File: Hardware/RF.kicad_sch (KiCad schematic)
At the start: 0 parts

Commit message: Checkpoint
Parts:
- added C2, C3, C4, C6, C7: 100nF, symbol Device:C_Small
- added C5: 47pF, symbol Device:C_Small
- added U3: SX1276, Package_DFN_QFN:QFN-28-1EP_6x6mm_P0.65mm_EP4.8x4.8mm, symbol RF:SX1276
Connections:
- new net: C6.1, U3.4 (VR_DIG)
- new net: C7.1, U3.2 (VR_ANA)
- new net DIO0: U3.8 (DIO0)
- new net DIO1: U3.9 (DIO1)
- new net DIO2: U3.10 (DIO2)
- new net DIO3: U3.11 (DIO3)
- new net DIO4: U3.12 (DIO4)
- new net DIO5: U3.13 (DIO5)
- new net GND: C2.1, C3.1, C4.1, C5.2, C6.2, C7.2, U3.15 (GND), U3.23 (GND), U3.26 (GND), U3.29 (GND)
- new net MISO: U3.17 (MISO)
- new net MOSI: U3.18 (MOSI)
- new net NSS: U3.19 (NSS)
- new net SCK: U3.16 (SCK)
- new net VDD: C2.2, C3.2, C4.2, C5.1, U3.14 (VBAT_DIG), U3.24 (VBAT_RF), U3.3 (VBAT_ANA)
- new net ~{RESET}: U3.7 (~{RESET})

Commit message: Checkpoint
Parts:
- renumbered C4 to C901, C3 to C902, C2 to C903, C5 to C904, C7 to C905, C6 to C906, U3 to U901
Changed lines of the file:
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@@
   (symbol (lib_id "Device:C_Small") (at 124.46 48.26 90) (unit 1)
     (in_bom yes) (on_board yes) (dnp no) (fields_autoplaced)
-    (property "Reference" "C3" (at 124.4663 41.91 90)
+    (property "Reference" "C902" (at 124.4663 41.91 90)
       (effects (font (size 1.27 1.27)))
     )
@@
       (project "Avionus_Flight_Controller"
         (path "/ddc7e940-0588-4587-8902-8ced9e615ace/a9aaa4a3-7ef9-4aeb-9917-54b44867eb01"
-          (reference "C3") (unit 1)
+          (reference "C902") (unit 1)
         )
       )
@@
   (symbol (lib_id "Device:C_Small") (at 144.78 58.42 90) (unit 1)
     (in_bom yes) (on_board yes) (dnp no) (fields_autoplaced)
-    (property "Reference" "C6" (at 144.7863 52.07 90)
+    (property "Reference" "C906" (at 144.7863 52.07 90)
       (effects (font (size 1.27 1.27)))
     )
@@
       (project "Avionus_Flight_Controller"
         (path "/ddc7e940-0588-4587-8902-8ced9e615ace/a9aaa4a3-7ef9-4aeb-9917-54b44867eb01"
-          (reference "C6") (unit 1)
+          (reference "C906") (unit 1)
         )
       )
@@
   (symbol (lib_id "RF:SX1276") (at 134.62 88.9 0) (unit 1)
     (in_bom yes) (on_board yes) (dnp no) (fields_autoplaced)
-    (property "Reference" "U3" (at 136.5759 116.84 0)
+    (property "Reference" "U901" (at 136.5759 116.84 0)
       (effects (font (size 1.27 1.27)) (justify left))
     )
@@
       (project "Avionus_Flight_Controller"
         (path "/ddc7e940-0588-4587-8902-8ced9e615ace/a9aaa4a3-7ef9-4aeb-9917-54b44867eb01"
-          (reference "U3") (unit 1)
+          (reference "U901") (unit 1)
         )
       )
@@
   (symbol (lib_id "Device:C_Small") (at 124.46 58.42 90) (unit 1)
     (in_bom yes) (on_board yes) (dnp no) (fields_autoplaced)
-    (property "Reference" "C2" (at 124.4663 52.07 90)
+    (property "Reference" "C903" (at 124.4663 52.07 90)
       (effects (font (size 1.27 1.27)))
     )
@@
       (project "Avionus_Flight_Controller"
         (path "/ddc7e940-0588-4587-8902-8ced9e615ace/a9aaa4a3-7ef9-4aeb-9917-54b44867eb01"
-          (reference "C2") (unit 1)
+          (reference "C903") (unit 1)
         )
       )
@@
   (symbol (lib_id "Device:C_Small") (at 124.46 38.1 90) (unit 1)
     (in_bom yes) (on_board yes) (dnp no) (fields_autoplaced)
-    (property "Reference" "C4" (at 124.4663 31.75 90)
+    (property "Reference" "C901" (at 124.4663 31.75 90)
       (effects (font (size 1.27 1.27)))
     )
@@
       (project "Avionus_Flight_Controller"
         (path "/ddc7e940-0588-4587-8902-8ced9e615ace/a9aaa4a3-7ef9-4aeb-9917-54b44867eb01"
-          (reference "C4") (unit 1)
+          (reference "C901") (unit 1)
         )
       )
@@
   (symbol (lib_id "Device:C_Small") (at 144.78 38.1 90) (unit 1)
     (in_bom yes) (on_board yes) (dnp no) (fields_autoplaced)
-    (property "Reference" "C5" (at 144.7863 31.75 90)
+    (property "Reference" "C904" (at 144.7863 31.75 90)
       (effects (font (size 1.27 1.27)))
     )
@@
       (project "Avionus_Flight_Controller"
         (path "/ddc7e940-0588-4587-8902-8ced9e615ace/a9aaa4a3-7ef9-4aeb-9917-54b44867eb01"
-          (reference "C5") (unit 1)
+          (reference "C904") (unit 1)
         )
       )
@@
   (symbol (lib_id "power:GND") (at 149.86 60.96 0) (unit 1)
     (in_bom yes) (on_board yes) (dnp no) (fields_autoplaced)
-    (property "Reference" "#PWR011" (at 149.86 67.31 0)
+    (property "Reference" "#PWR0903" (at 149.86 67.31 0)
       (effects (font (size 1.27 1.27)) hide)
     )
@@
       (project "Avionus_Flight_Controller"
         (path "/ddc7e940-0588-4587-8902-8ced9e615ace/a9aaa4a3-7ef9-4aeb-9917-54b44867eb01"
-          (reference "#PWR011") (unit 1)
+          (reference "#PWR0903") (unit 1)
         )
       )
@@
   (symbol (lib_id "power:GND") (at 119.38 60.96 0) (unit 1)
     (in_bom yes) (on_board yes) (dnp no) (fields_autoplaced)
-    (property "Reference" "#PWR010" (at 119.38 67.31 0)
+    (property "Reference" "#PWR0901" (at 119.38 67.31 0)
       (effects (font (size 1.27 1.27)) hide)
     )
@@
       (project "Avionus_Flight_Controller"
         (path "/ddc7e940-0588-4587-8902-8ced9e615ace/a9aaa4a3-7ef9-4aeb-9917-54b44867eb01"
-          (reference "#PWR010") (unit 1)
+          (reference "#PWR0901") (unit 1)
         )
       )
@@
   (symbol (lib_id "Device:C_Small") (at 144.78 48.26 90) (unit 1)
     (in_bom yes) (on_board yes) (dnp no) (fields_autoplaced)
-    (property "Reference" "C7" (at 144.7863 41.91 90)
+    (property "Reference" "C905" (at 144.7863 41.91 90)
       (effects (font (size 1.27 1.27)))
     )
@@
       (project "Avionus_Flight_Controller"
         (path "/ddc7e940-0588-4587-8902-8ced9e615ace/a9aaa4a3-7ef9-4aeb-9917-54b44867eb01"
-          (reference "C7") (unit 1)
+          (reference "C905") (unit 1)
         )
       )
@@
   (symbol (lib_id "power:GND") (at 134.62 116.84 0) (unit 1)
     (in_bom yes) (on_board yes) (dnp no) (fields_autoplaced)
-    (property "Reference" "#PWR07" (at 134.62 123.19 0)
+    (property "Reference" "#PWR0902" (at 134.62 123.19 0)
       (effects (font (size 1.27 1.27)) hide)
     )
@@
       (project "Avionus_Flight_Controller"
         (path "/ddc7e940-0588-4587-8902-8ced9e615ace/a9aaa4a3-7ef9-4aeb-9917-54b44867eb01"
-          (reference "#PWR07") (unit 1)
-        )
-      )
+          (reference "#PWR0902") (unit 1)
+        )
+      )

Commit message: Checkpoint
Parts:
- added C901, C902: 18pF, Capacitor_SMD:C_0402_1005Metric, symbol Device:C_Small
- added TP901: RXTX, symbol Connector:TestPoint
- added Y901: 24MHz, Crystal:Crystal_SMD_2016-4Pin_2.0x1.6mm, symbol Device:Crystal_GND24_Small
- C903: renamed from C901; footprint (none) -> Capacitor_SMD:C_0603_1608Metric
- C904: renamed from C902; footprint (none) -> Capacitor_SMD:C_0603_1608Metric
- C905: renamed from C903; footprint (none) -> Capacitor_SMD:C_0603_1608Metric
- C906: renamed from C904; value 47pF -> 51pF; footprint (none) -> Capacitor_SMD:C_0402_1005Metric
- C907: renamed from C905; footprint (none) -> Capacitor_SMD:C_0603_1608Metric
- C908: renamed from C906; footprint (none) -> Capacitor_SMD:C_0603_1608Metric
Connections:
- net GND: now also C901.1, C902.1, Y901.2, Y901.4
- net at U901.20 (RXTX/RF_MOD): now also TP901.1
- net at U901.5 (XTA): now also C901.2, Y901.3
- net at U901.6 (XTB): now also C902.2, Y901.1
- no-connect marks 0 -> 2

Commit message: Checkpoint
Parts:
- TP901: value RXTX -> ~; footprint (none) -> TestPoint:TestPoint_Pad_D2.0mm
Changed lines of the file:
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@@
   (symbol (lib_id "Connector:TestPoint") (at 149.86 104.14 270) (unit 1)
     (in_bom yes) (on_board yes) (dnp no) (fields_autoplaced)
-    (property "Reference" "TP901" (at 154.94 102.87 90)
+    (property "Reference" "TP901" (at 154.94 104.14 90)
       (effects (font (size 1.27 1.27)) (justify left))
     )
-    (property "Value" "RXTX" (at 154.94 105.41 90)
+    (property "Value" "~" (at 154.94 105.41 90)
       (effects (font (size 1.27 1.27)) (justify left))
     )
-    (property "Footprint" "" (at 149.86 109.22 0)
+    (property "Footprint" "TestPoint:TestPoint_Pad_D2.0mm" (at 149.86 109.22 0)
       (effects (font (size 1.27 1.27)) hide)
     )

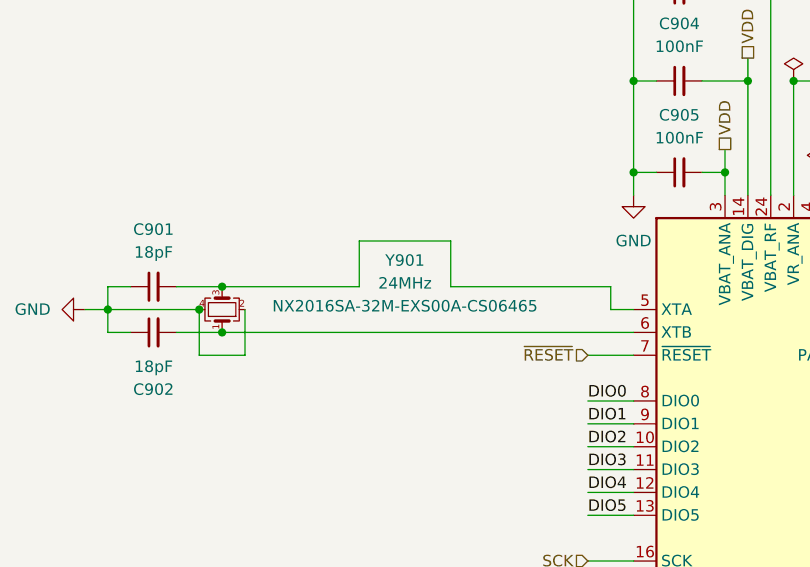
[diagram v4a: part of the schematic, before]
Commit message: Fix RF crystal frequency
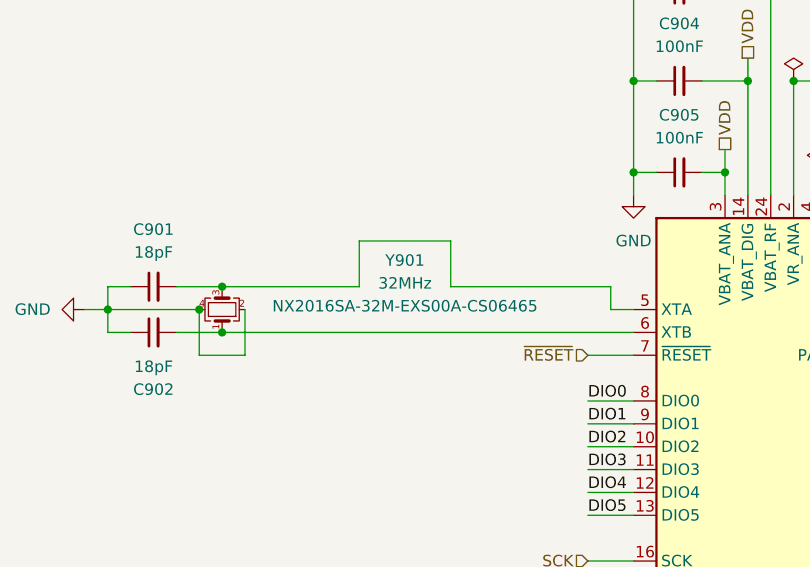
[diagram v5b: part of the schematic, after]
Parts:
- Y901: value 24MHz -> 32MHz
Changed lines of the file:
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@@
       (effects (font (size 1.27 1.27)))
     )
-    (property "Value" "24MHz" (at 93.98 70.7457 90)
+    (property "Value" "32MHz" (at 93.98 70.7457 90)
       (effects (font (size 1.27 1.27)))
     )

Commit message: Checkpoint
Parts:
- added C909: 100pF, symbol Device:C_Small
- added C910: 47pF, symbol Device:C_Small
- added C911: 10nF, symbol Device:C_Small
- added R901: 1K, symbol Device:R_Small
- added U902: PE42421SCAA-Z, Package_TO_SOT_SMD:SOT-363_SC-70-6, symbol RF_Switch:MASWSS0136
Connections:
- net GND: now also C909.2, C910.2, C911.2, U902.2 (GND)
- net VDD: now also U902.6 (V1)
- net RXTX: now reaches TP901.1, U901.20 (RXTX/RF_MOD)
- net RXTX: now also R901.2
- net RFI_HF: now reaches U901.21 (RFI_HF)
- net at U901.25 (VR_PA): now also C909.1, C910.1, C911.1
- net PA_BOOST: now reaches U901.27 (PA_BOOST)
- new net: R901.1, U902.4 (V2)
- no-connect marks 2 -> 3
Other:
- note added: "RX"
- note added: "TX"
- moved on the sheet: TP901

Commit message: Checkpoint
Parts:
- removed C901, C902: 18pF, Capacitor_SMD:C_0402_1005Metric, symbol Device:C_Small
- removed C903, C904, C905, C907, C908: 100nF, Capacitor_SMD:C_0603_1608Metric, symbol Device:C_Small
- removed C906: 51pF, Capacitor_SMD:C_0402_1005Metric, symbol Device:C_Small
- removed C909: 100pF, symbol Device:C_Small
- removed C910: 47pF, symbol Device:C_Small
- removed C911: 10nF, symbol Device:C_Small
- removed R901: 1K, symbol Device:R_Small
- removed TP901: ~, TestPoint:TestPoint_Pad_D2.0mm, symbol Connector:TestPoint
- removed U901: SX1276, Package_DFN_QFN:QFN-28-1EP_6x6mm_P0.65mm_EP4.8x4.8mm, symbol RF:SX1276
- removed U902: PE42421SCAA-Z, Package_TO_SOT_SMD:SOT-363_SC-70-6, symbol RF_Switch:MASWSS0136
- removed Y901: 32MHz, Crystal:Crystal_SMD_2016-4Pin_2.0x1.6mm, symbol Device:Crystal_GND24_Small
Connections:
- no-connect marks 3 -> 0
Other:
- note removed: "RX"
- note removed: "TX"

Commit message: Checkpoint
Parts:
- added J901: ~, Connector_Coaxial:SMA_Amphenol_132134_Vertical, symbol Connector:Conn_Coaxial
- added U901: LAMBDA62, leptunKicadLib:LAMBDA62, symbol leptunKicadLib:LAMBDA62
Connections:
- net BUSY: now also U901.6 (BUSY)
- net DIO1: now also U901.7 (DIO1)
- net DIO2: now also U901.8 (DIO2)
- net DIO3: now also U901.9 (DIO3)
- net MISO: now also U901.14 (MISO)
- net MOSI: now also U901.15 (MOSI)
- net NSS: now also U901.16 (NSS)
- net RX_SWITCH: now also U901.4 (RX_SWITCH)
- net SCK: now also U901.13 (SCK)
- net TX_SWITCH: now also U901.5 (TX_SWITCH)
- net VDD: now also U901.3 (VCC)
- net ~{RESET}: now also U901.12 (~{RESET})
- new net: J901.1 (In), U901.1 (ANT/NC)
- new net GND: J901.2 (Ext), U901.2 (GND)
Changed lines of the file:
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@@
 (kicad_sch (version 20230121) (generator eeschema)
   (paper "A4")
-  (wire (pts (xy 114.3 86.36) (xy 119.38 86.36))
+  (wire (pts (xy 162.56 83.82) (xy 175.26 83.82))
     (stroke (width 0) (type default))
   )
-  (wire (pts (xy 114.3 78.74) (xy 119.38 78.74))
-    (stroke (width 0) (type default))
+  (hierarchical_label "TX_SWITCH" (shape input) (at 162.56 111.76 0) (fields_autoplaced)
+    (effects (font (size 1.27 1.27)) (justify left))
   )
-  (wire (pts (xy 114.3 96.52) (xy 119.38 96.52))
-    (stroke (width 0) (type default))
+  (hierarchical_label "RX_SWITCH" (shape input) (at 162.56 109.22 0) (fields_autoplaced)
+    (effects (font (size 1.27 1.27)) (justify left))
   )
-  (wire (pts (xy 114.3 91.44) (xy 119.38 91.44))
-    (stroke (width 0) (type default))
-  )
-  (wire (pts (xy 114.3 88.9) (xy 119.38 88.9))
-    (stroke (width 0) (type default))
-  )
-  (wire (pts (xy 114.3 101.6) (xy 119.38 101.6))
-    (stroke (width 0) (type default))
-  )
-  (wire (pts (xy 114.3 93.98) (xy 119.38 93.98))
-    (stroke (width 0) (type default))
-  )
-  (wire (pts (xy 114.3 109.22) (xy 119.38 109.22))
-    (stroke (width 0) (type default))
-  )
-  (wire (pts (xy 114.3 104.14) (xy 119.38 104.14))
-    (stroke (width 0) (type default))
-  )
-  (wire (pts (xy 114.3 106.68) (xy 119.38 106.68))
-    (stroke (width 0) (type default))
-  )
-  (wire (pts (xy 114.3 83.82) (xy 119.38 83.82))
-    (stroke (width 0) (type default))
-  )
-  (hierarchical_label "TX_SWITCH" (shape input) (at 114.3 86.36 180) (fields_autoplaced)
+  (hierarchical_label "MOSI" (shape input) (at 132.08 111.76 180) (fields_autoplaced)
     (effects (font (size 1.27 1.27)) (justify right))
   )
-  (hierarchical_label "RX_SWITCH" (shape input) (at 114.3 83.82 180) (fields_autoplaced)
+  (hierarchical_label "NSS" (shape input) (at 132.08 114.3 180) (fields_autoplaced)
     (effects (font (size 1.27 1.27)) (justify right))
   )
-  (hierarchical_label "MOSI" (shape input) (at 114.3 106.68 180) (fields_autoplaced)
+  (hierarchical_label "~{RESET}" (shape input) (at 132.08 83.82 180) (fields_autoplaced)
     (effects (font (size 1.27 1.27)) (justify right))
   )
-  (hierarchical_label "NSS" (shape input) (at 114.3 109.22 180) (fields_autoplaced)
+  (hierarchical_label "MISO" (shape output) (at 132.08 109.22 180) (fields_autoplaced)
     (effects (font (size 1.27 1.27)) (justify right))
   )
-  (hierarchical_label "~{RESET}" (shape input) (at 114.3 78.74 180) (fields_autoplaced)
+  (hierarchical_label "DIO2" (shape output) (at 132.08 93.98 180) (fields_autoplaced)
     (effects (font (size 1.27 1.27)) (justify right))
   )
-  (hierarchical_label "MISO" (shape output) (at 114.3 104.14 180) (fields_autoplaced)
+  (hierarchical_label "VDD" (shape passive) (at 147.32 66.04 90) (fields_autoplaced)
+    (effects (font (size 1.27 1.27)) (justify left))
+  )
+  (hierarchical_label "SCK" (shape input) (at 132.08 106.68 180) (fields_autoplaced)
     (effects (font (size 1.27 1.27)) (justify right))
   )
-  (hierarchical_label "DIO2" (shape output) (at 114.3 91.44 180) (fields_autoplaced)
+  (hierarchical_label "DIO1" (shape output) (at 132.08 91.44 180) (fields_autoplaced)
     (effects (font (size 1.27 1.27)) (justify right))
   )
-  (hierarchical_label "VDD" (shape passive) (at 119.38 73.66 180) (fields_autoplaced)
+  (hierarchical_label "DIO3" (shape output) (at 132.08 96.52 180) (fields_autoplaced)
     (effects (font (size 1.27 1.27)) (justify right))
   )
-  (hierarchical_label "SCK" (shape input) (at 114.3 101.6 180) (fields_autoplaced)
+  (hierarchical_label "BUSY" (shape output) (at 132.08 88.9 180) (fields_autoplaced)
     (effects (font (size 1.27 1.27)) (justify right))
   )
-  (hierarchical_label "DIO1" (shape output) (at 114.3 93.98 180) (fields_autoplaced)
-    (effects (font (size 1.27 1.27)) (justify right))
+  (symbol (lib_id "power:GND") (at 180.34 88.9 0) (unit 1)
+    (in_bom yes) (on_board yes) (dnp no) (fields_autoplaced)
+    (property "Reference" "#PWR0902" (at 180.34 95.25 0)
+      (effects (font (size 1.27 1.27)) hide)
+    )
+    (property "Value" "GND" (at 180.34 93.98 0)
+      (effects (font (size 1.27 1.27)))
+    )
+    (property "Footprint" "" (at 180.34 88.9 0)
+      (effects (font (size 1.27 1.27)) hide)
+    )
+    (property "Datasheet" "" (at 180.34 88.9 0)
+      (effects (font (size 1.27 1.27)) hide)
+    )
+    (pin "1")
+    (instances
+      (project "Avionus_Flight_Controller"
+        (path "/ddc7e940-0588-4587-8902-8ced9e615ace/a9aaa4a3-7ef9-4aeb-9917-54b44867eb01"
+          (reference "#PWR0902") (unit 1)
+        )
+      )
+    )
   )
-  (hierarchical_label "DIO3" (shape output) (at 114.3 88.9 180) (fields_autoplaced)
-    (effects (font (size 1.27 1.27)) (justify right))
+  (symbol (lib_id "Connector:Conn_Coaxial") (at 180.34 83.82 0) (unit 1)
+    (in_bom yes) (on_board yes) (dnp no) (fields_autoplaced)
+    (property "Reference" "J901" (at 184.15 84.1132 0)
+      (effects (font (size 1.27 1.27)) (justify left))
+    )
+    (property "Value" "~" (at 184.15 85.3832 0)
+      (effects (font (size 1.27 1.27)) (justify left))
+    )
+    (property "Footprint" "Connector_Coaxial:SMA_Amphenol_132134_Vertical" (at 180.34 83.82 0)
+      (effects (font (size 1.27 1.27)) hide)
+    )
+    (property "Datasheet" " ~" (at 180.34 83.82 0)
+      (effects (font (size 1.27 1.27)) hide)
+    )
+    (pin "1")
+    (pin "2")
+    (instances
+      (project "Avionus_Flight_Controller"
+        (path "/ddc7e940-0588-4587-8902-8ced9e615ace/a9aaa4a3-7ef9-4aeb-9917-54b44867eb01"
+          (reference "J901") (unit 1)
+        )
+      )
+    )
   )
-  (hierarchical_label "BUSY" (shape output) (at 114.3 96.52 180) (fields_autoplaced)
-    (effects (font (size 1.27 1.27)) (justify right))
+  (symbol (lib_id "leptunKicadLib:LAMBDA62") (at 147.32 93.98 0) (unit 1)
+    (in_bom yes) (on_board yes) (dnp no) (fields_autoplaced)
+    (property "Reference" "U901" (at 149.5141 63.5 0)
+      (effects (font (size 1.27 1.27)) (justify left))
+    )
+    (property "Value" "LAMBDA62" (at 149.5141 66.04 0)
+      (effects (font (size 1.27 1.27)) (justify left))
+    )
+    (property "Footprint" "leptunKicadLib:LAMBDA62" (at 147.32 101.6 0)
+      (effects (font (size 1.27 1.27)) hide)
+    )
+    (property "Datasheet" "https://www.rfsolutions.co.uk/downloads/63c81a2964da3203DS-LAMBDA62-6.pdf" (at 147.32 99.06 0)
+      (effects (font (size 1.27 1.27)) hide)
+    )
+    (pin "1")
+    (pin "10")
+    (pin "11")
+    (pin "12")
+    (pin "13")
+    (pin "14")
+    (pin "15")
+    (pin "16")
+    (pin "2")
+    (pin "3")
+    (pin "4")
+    (pin "5")
+    (pin "6")
+    (pin "7")
+    (pin "8")
+    (pin "9")
+    (instances
+      (project "Avionus_Flight_Controller"
+        (path "/ddc7e940-0588-4587-8902-8ced9e615ace/a9aaa4a3-7ef9-4aeb-9917-54b44867eb01"
+          (reference "U901") (unit 1)
+        )
+      )
+    )
+  )
+  (symbol (lib_id "power:GND") (at 147.32 121.92 0) (unit 1)
+    (in_bom yes) (on_board yes) (dnp no) (fields_autoplaced)
+    (property "Reference" "#PWR0901" (at 147.32 128.27 0)
+      (effects (font (size 1.27 1.27)) hide)
+    )
+    (property "Value" "GND" (at 147.32 127 0)
+      (effects (font (size 1.27 1.27)))
+    )
+    (property "Footprint" "" (at 147.32 121.92 0)
+      (effects (font (size 1.27 1.27)) hide)
+    )
+    (property "Datasheet" "" (at 147.32 121.92 0)
+      (effects (font (size 1.27 1.27)) hide)
+    )
+    (pin "1")
+    (instances
+      (project "Avionus_Flight_Controller"
+        (path "/ddc7e940-0588-4587-8902-8ced9e615ace/a9aaa4a3-7ef9-4aeb-9917-54b44867eb01"
+          (reference "#PWR0901") (unit 1)
+        )
+      )
+    )
   )
 )
